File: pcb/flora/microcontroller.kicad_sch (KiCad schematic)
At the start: 14 parts, among them IC1 ESP32-WROOM-32E(8MB), Q1 MUN5214DW1T1G

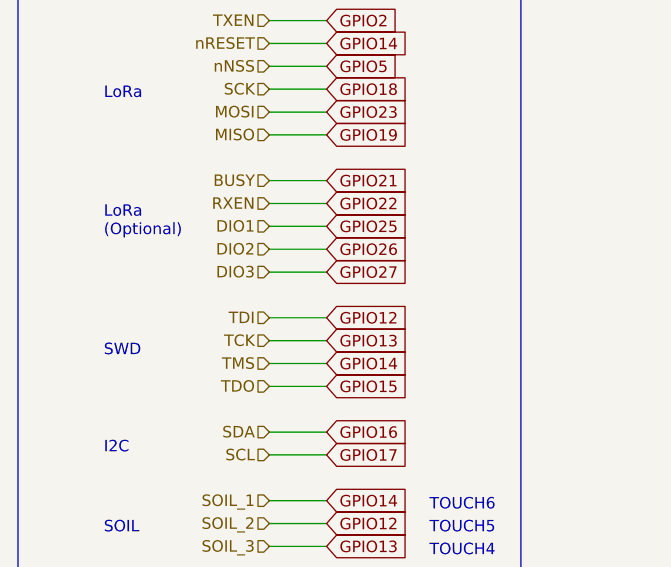
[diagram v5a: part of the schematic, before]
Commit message: Finished schematic for RA-01 design
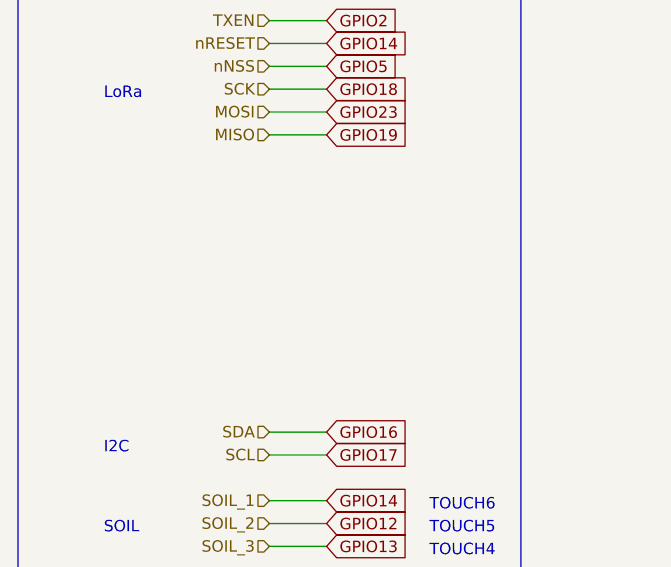
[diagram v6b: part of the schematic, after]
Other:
- note removed: "LoRa (Optional)"
- note removed: "SWD"
- title: FLORA -> FLORA-RA01H
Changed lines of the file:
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@@
   (paper "A3")
   (title_block
-    (title "FLORA")
-    (date "2022-07-01")
+    (title "FLORA-RA01H")
+    (date "2022-12-05")
     (rev "C")
   )
@@
     (stroke (width 0) (type default) (color 0 0 0 0))
   )
-  (wire (pts (xy 83.82 186.69) (xy 90.17 186.69))
-    (stroke (width 0) (type default) (color 0 0 0 0))
-  )
   (wire (pts (xy 227.965 189.865) (xy 227.965 191.77))
     (stroke (width 0) (type default) (color 0 0 0 0))
@@
     (stroke (width 0) (type default) (color 0 0 0 0))
   )
-  (wire (pts (xy 83.82 181.61) (xy 90.17 181.61))
-    (stroke (width 0) (type default) (color 0 0 0 0))
-  )
   (wire (pts (xy 205.74 167.005) (xy 210.185 167.005))
     (stroke (width 0) (type default) (color 0 0 0 0))
@@
     (stroke (width 0) (type default) (color 0 0 0 0))
   )
-  (wire (pts (xy 83.82 179.07) (xy 90.17 179.07))
-    (stroke (width 0) (type default) (color 0 0 0 0))
-  )
   (wire (pts (xy 205.74 164.465) (xy 210.185 164.465))
     (stroke (width 0) (type default) (color 0 0 0 0))
@@
     (stroke (width 0) (type default) (color 0 0 0 0))
   )
-  (wire (pts (xy 83.82 199.39) (xy 90.17 199.39))
-    (stroke (width 0) (type default) (color 0 0 0 0))
-  )
   (wire (pts (xy 240.665 189.865) (xy 240.665 191.77))
     (stroke (width 0) (type default) (color 0 0 0 0))
@@
     (stroke (width 0) (type default) (color 0 0 0 0))
   )
-  (wire (pts (xy 83.82 191.77) (xy 90.17 191.77))
-    (stroke (width 0) (type default) (color 0 0 0 0))
-  )
   (wire (pts (xy 273.05 159.385) (xy 268.605 159.385))
     (stroke (width 0) (type default) (color 0 0 0 0))
@@
     (stroke (width 0) (type default) (color 0 0 0 0))
   )
-  (wire (pts (xy 83.82 176.53) (xy 90.17 176.53))
-    (stroke (width 0) (type default) (color 0 0 0 0))
-  )
   (wire (pts (xy 328.295 174.625) (xy 328.295 176.53))
     (stroke (width 0) (type default) (color 0 0 0 0))
@@
     (stroke (width 0) (type default) (color 0 0 0 0))
   )
-  (wire (pts (xy 83.82 184.15) (xy 90.17 184.15))
-    (stroke (width 0) (type default) (color 0 0 0 0))
-  )
   (wire (pts (xy 350.52 127.635) (xy 361.188 127.635))
     (stroke (width 0) (type default) (color 0 0 0 0))
@@
     (stroke (width 0) (type default) (color 0 0 0 0))
   )
-  (wire (pts (xy 83.82 196.85) (xy 90.17 196.85))
-    (stroke (width 0) (type default) (color 0 0 0 0))
-  )
   (wire (pts (xy 235.585 191.77) (xy 238.125 191.77))
     (stroke (width 0) (type default) (color 0 0 0 0))
   )
-  (wire (pts (xy 83.82 194.31) (xy 90.17 194.31))
-    (stroke (width 0) (type default) (color 0 0 0 0))
-  )
   (wire (pts (xy 352.425 161.29) (xy 347.98 161.29))
     (stroke (width 0) (type default) (color 0 0 0 0))
@@
   )
   (text "MICROCONTROLLER" (at 226.695 80.01 0)
-    (effects (font (size 1.27 1.27)) (justify left bottom))
-  )
-  (text "SWD" (at 65.405 196.215 0)
-    (effects (font (size 1.27 1.27)) (justify left bottom))
-  )
-  (text "LoRa\n(Optional)" (at 65.405 182.88 0)
     (effects (font (size 1.27 1.27)) (justify left bottom))
   )
@@
     )
   )
-  (global_label "GPIO14" (shape input) (at 90.17 196.85 0) (fields_autoplaced)
-    (effects (font (size 1.27 1.27)) (justify left))
-    (property "Intersheet References" "${INTERSHEET_REFS}" (id 0) (at 99.4774 196.7706 0)
-      (effects (font (size 1.27 1.27)) (justify left) hide)
-    )
-  )
   (global_label "GPIO25" (shape input) (at 273.05 164.465 0) (fields_autoplaced)
     (effects (font (size 1.27 1.27)) (justify left))
@@
     )
   )
-  (global_label "GPIO27" (shape input) (at 90.17 186.69 0) (fields_autoplaced)
-    (effects (font (size 1.27 1.27)) (justify left))
-    (property "Intersheet References" "${INTERSHEET_REFS}" (id 0) (at 99.4774 186.6106 0)
-      (effects (font (size 1.27 1.27)) (justify left) hide)
-    )
-  )
   (global_label "GPIO15" (shape input) (at 273.05 144.145 0) (fields_autoplaced)
     (effects (font (size 1.27 1.27)) (justify left))
@@
     )
   )
-  (global_label "GPIO26" (shape input) (at 90.17 184.15 0) (fields_autoplaced)
-    (effects (font (size 1.27 1.27)) (justify left))
-    (property "Intersheet References" "${INTERSHEET_REFS}" (id 0) (at 99.4774 184.0706 0)
-      (effects (font (size 1.27 1.27)) (justify left) hide)
-    )
-  )
-  (global_label "GPIO13" (shape input) (at 90.17 194.31 0) (fields_autoplaced)
-    (effects (font (size 1.27 1.27)) (justify left))
-    (property "Intersheet References" "${INTERSHEET_REFS}" (id 0) (at 99.4774 194.2306 0)
-      (effects (font (size 1.27 1.27)) (justify left) hide)
-    )
-  )
-  (global_label "GPIO25" (shape input) (at 90.17 181.61 0) (fields_autoplaced)
-    (effects (font (size 1.27 1.27)) (justify left))
-    (property "Intersheet References" "${INTERSHEET_REFS}" (id 0) (at 99.4774 181.5306 0)
-      (effects (font (size 1.27 1.27)) (justify left) hide)
-    )
-  )
   (global_label "GPIO12" (shape input) (at 90.17 214.63 0) (fields_autoplaced)
     (effects (font (size 1.27 1.27)) (justify left))
@@
     )
   )
-  (global_label "GPIO15" (shape input) (at 90.17 199.39 0) (fields_autoplaced)
-    (effects (font (size 1.27 1.27)) (justify left))
-    (property "Intersheet References" "${INTERSHEET_REFS}" (id 0) (at 99.4774 199.3106 0)
-      (effects (font (size 1.27 1.27)) (justify left) hide)
-    )
-  )
   (global_label "GPIO17" (shape input) (at 90.17 207.01 0) (fields_autoplaced)
     (effects (font (size 1.27 1.27)) (justify left))
@@
     )
   )
-  (global_label "GPIO21" (shape input) (at 90.17 176.53 0) (fields_autoplaced)
-    (effects (font (size 1.27 1.27)) (justify left))
-    (property "Intersheet References" "${INTERSHEET_REFS}" (id 0) (at 99.4774 176.4506 0)
-      (effects (font (size 1.27 1.27)) (justify left) hide)
-    )
-  )
   (global_label "GPIO12" (shape input) (at 273.05 136.525 0) (fields_autoplaced)
     (effects (font (size 1.27 1.27)) (justify left))
@@
     (effects (font (size 1.27 1.27)) (justify left))
     (property "Intersheet References" "${INTERSHEET_REFS}" (id 0) (at 366.0806 94.5356 0)
-      (effects (font (size 1.27 1.27)) (justify left) hide)
-    )
-  )
-  (global_label "GPIO22" (shape input) (at 90.17 179.07 0) (fields_autoplaced)
-    (effects (font (size 1.27 1.27)) (justify left))
-    (property "Intersheet References" "${INTERSHEET_REFS}" (id 0) (at 99.4774 178.9906 0)
       (effects (font (size 1.27 1.27)) (justify left) hide)
     )
@@
     )
   )
-  (global_label "GPIO12" (shape input) (at 90.17 191.77 0) (fields_autoplaced)
-    (effects (font (size 1.27 1.27)) (justify left))
-    (property "Intersheet References" "${INTERSHEET_REFS}" (id 0) (at 99.4774 191.6906 0)
-      (effects (font (size 1.27 1.27)) (justify left) hide)
-    )
-  )
   (global_label "GPIO0" (shape input) (at 352.425 184.785 0) (fields_autoplaced)
     (effects (font (size 1.27 1.27)) (justify left))
@@
     (effects (font (size 1.27 1.27)) (justify right))
   )
-  (hierarchical_label "RXEN" (shape input) (at 83.82 179.07 180)
-    (effects (font (size 1.27 1.27)) (justify right))
-  )
   (hierarchical_label "U0TXD" (shape input) (at 205.74 164.465 180)
     (effects (font (size 1.27 1.27)) (justify right))
@@
     (effects (font (size 1.27 1.27)) (justify right))
   )
-  (hierarchical_label "DIO3" (shape input) (at 83.82 186.69 180)
-    (effects (font (size 1.27 1.27)) (justify right))
-  )
-  (hierarchical_label "TDO" (shape input) (at 83.82 199.39 180)
-    (effects (font (size 1.27 1.27)) (justify right))
-  )
   (hierarchical_label "SCL" (shape input) (at 83.82 207.01 180)
     (effects (font (size 1.27 1.27)) (justify right))
@@
     (effects (font (size 1.27 1.27)) (justify right))
   )
-  (hierarchical_label "BUSY" (shape input) (at 83.82 176.53 180)
-    (effects (font (size 1.27 1.27)) (justify right))
-  )
-  (hierarchical_label "TCK" (shape input) (at 83.82 194.31 180)
-    (effects (font (size 1.27 1.27)) (justify right))
-  )
   (hierarchical_label "nRESET" (shape input) (at 83.82 161.29 180)
     (effects (font (size 1.27 1.27)) (justify right))
   )
-  (hierarchical_label "DIO2" (shape input) (at 83.82 184.15 180)
-    (effects (font (size 1.27 1.27)) (justify right))
-  )
-  (hierarchical_label "DIO1" (shape input) (at 83.82 181.61 180)
-    (effects (font (size 1.27 1.27)) (justify right))
-  )
   (hierarchical_label "TXEN" (shape input) (at 83.82 158.75 180)
     (effects (font (size 1.27 1.27)) (justify right))
   )
-  (hierarchical_label "TDI" (shape input) (at 83.82 191.77 180)
-    (effects (font (size 1.27 1.27)) (justify right))
-  )
-  (hierarchical_label "TMS" (shape input) (at 83.82 196.85 180)
-    (effects (font (size 1.27 1.27)) (justify right))
-  )
